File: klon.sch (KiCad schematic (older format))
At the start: 71 parts, among them SW1 SW_DPDT_x2, U1 TL072, U2 LTC1044, U3 TL072

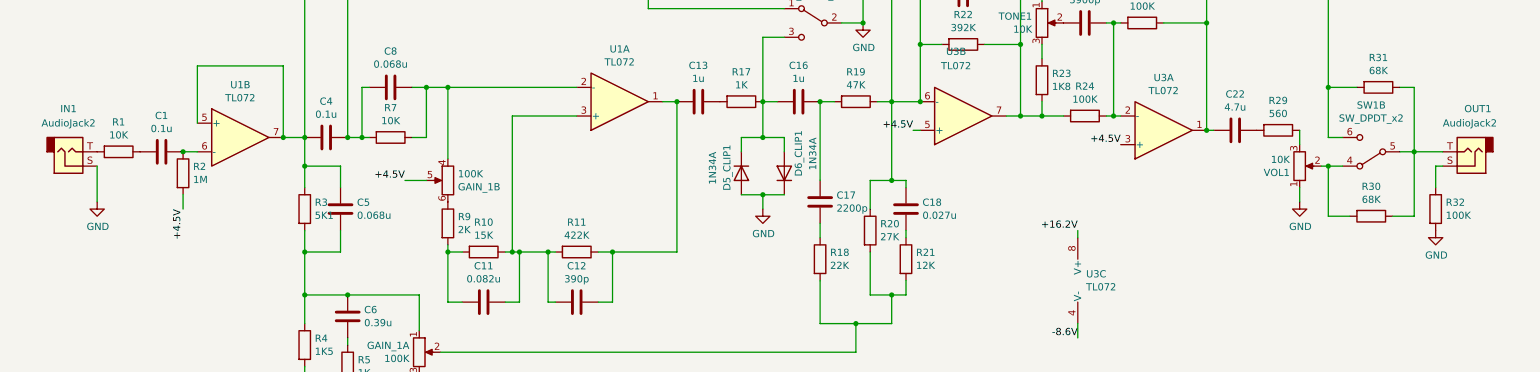
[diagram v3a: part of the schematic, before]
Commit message: add custom models, change pcb board layout
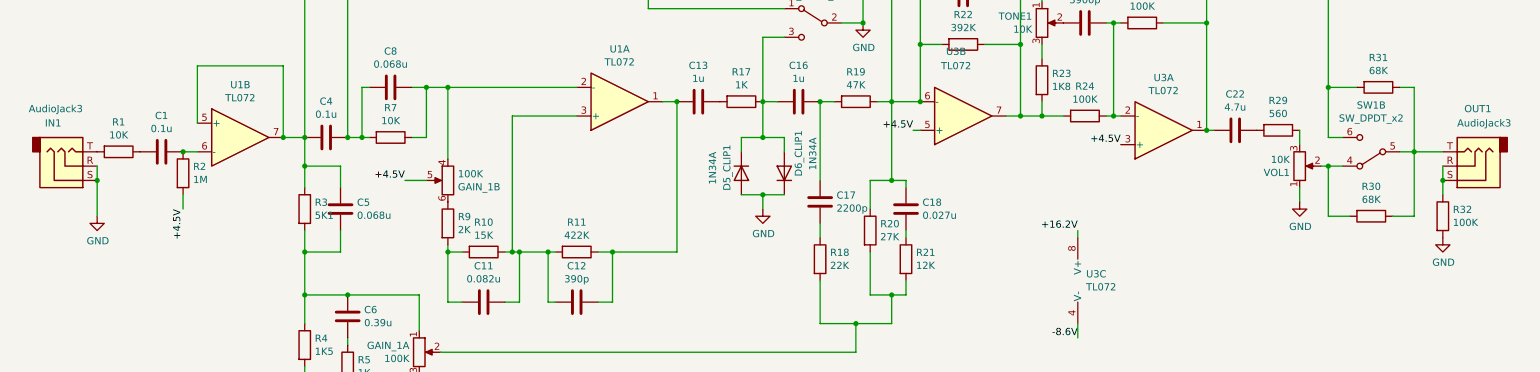
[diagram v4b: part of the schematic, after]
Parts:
- removed IN1, OUT1: AudioJack2, Connector_Audio:Jack_6.35mm_Neutrik_NMJ4HFD2_Horizontal, symbol Connector:AudioJack2
- added IN1, OUT1: AudioJack3, Connector_Audio:Jack_6.35mm_Neutrik_NMJ6HFD2_Horizontal, symbol Connector:AudioJack3
- GAIN_1: footprint Connector_PinHeader_1.27mm:PinHeader_2x03_P1.27mm_Vertical -> Potentiometer_THT:Potentiometer_Alpha_RD902F-40-00D_Dual_Vertical_CircularHoles
- TONE1, VOL1: footprint Connector_PinHeader_1.27mm:PinHeader_1x03_P1.27mm_Vertical -> Potentiometer_THT:Potentiometer_Alpha_RD901F-40-00D_Single_Vertical_CircularHoles
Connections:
- net GND: now also IN1.R, IN1.S
- net at R1.2: now also IN1.T
- net at R30.1, R31.1, SW1.5 (B): now also OUT1.T
- net at R32.1: now also OUT1.R, OUT1.S
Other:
- moved on the sheet: R32
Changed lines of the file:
@@
 F 0 "GAIN_1" H 3281 4846 50  0000 R CNN
 F 1 "100K" H 3281 4755 50  0000 R CNN
-F 2 "Connector_PinHeader_1.27mm:PinHeader_2x03_P1.27mm_Vertical" H 3350 4800 50  0001 C CNN
+F 2 "Potentiometer_THT:Potentiometer_Alpha_RD902F-40-00D_Dual_Vertical_CircularHoles" H 3350 4800 50  0001 C CNN
 F 3 "~" H 3350 4800 50  0001 C CNN
 	1    3350 4800
@@
 F 0 "TONE1" H 7631 2546 50  0000 R CNN
 F 1 "10K" H 7631 2455 50  0000 R CNN
-F 2 "Connector_PinHeader_1.27mm:PinHeader_1x03_P1.27mm_Vertical" H 7700 2500 50  0001 C CNN
+F 2 "Potentiometer_THT:Potentiometer_Alpha_RD901F-40-00D_Single_Vertical_CircularHoles" H 7700 2500 50  0001 C CNN
 F 3 "~" H 7700 2500 50  0001 C CNN
 	1    7700 2500
@@
 F 0 "VOL1" H 9431 3546 50  0000 R CNN
 F 1 "10K" H 9431 3455 50  0000 R CNN
-F 2 "Connector_PinHeader_1.27mm:PinHeader_1x03_P1.27mm_Vertical" H 9500 3500 50  0001 C CNN
+F 2 "Potentiometer_THT:Potentiometer_Alpha_RD901F-40-00D_Single_Vertical_CircularHoles" H 9500 3500 50  0001 C CNN
 F 3 "~" H 9500 3500 50  0001 C CNN
 	1    9500 3500
@@
 L Device:R R32
 U 1 1 60E3FE02
-P 10450 3800
-F 0 "R32" H 10520 3846 50  0000 L CNN
-F 1 "100K" H 10520 3755 50  0000 L CNN
-F 2 "Resistor_THT:R_Axial_DIN0207_L6.3mm_D2.5mm_P10.16mm_Horizontal" V 10380 3800 50  0001 C CNN
-F 3 "~" H 10450 3800 50  0001 C CNN
-	1    10450 3800
+P 10500 3850
+F 0 "R32" H 10570 3896 50  0000 L CNN
+F 1 "100K" H 10570 3805 50  0000 L CNN
+F 2 "Resistor_THT:R_Axial_DIN0207_L6.3mm_D2.5mm_P10.16mm_Horizontal" V 10430 3850 50  0001 C CNN
+F 3 "~" H 10500 3850 50  0001 C CNN
+	1    10500 3850
 	1    0    0    -1
 $EndComp
@@
 L power:GND #PWR017
 U 1 1 60E40ABE
-P 10450 3950
-F 0 "#PWR017" H 10450 3700 50  0001 C CNN
-F 1 "GND" H 10455 3777 50  0000 C CNN
-F 2 "" H 10450 3950 50  0001 C CNN
-F 3 "" H 10450 3950 50  0001 C CNN
-	1    10450 3950
+P 10500 4000
+F 0 "#PWR017" H 10500 3750 50  0001 C CNN
+F 1 "GND" H 10505 3827 50  0000 C CNN
+F 2 "" H 10500 4000 50  0001 C CNN
+F 3 "" H 10500 4000 50  0001 C CNN
+	1    10500 4000
 	1    0    0    -1
 $EndComp
@@
 Wire Wire Line
 	10150 3850 10300 3850
-$Comp
-L Connector:AudioJack2 OUT1
-U 1 1 60F6182B
-P 10700 3400
-F 0 "OUT1" H 10750 3100 50  0000 R CNN
-F 1 "AudioJack2" H 10900 3200 50  0000 R CNN
-F 2 "Connector_Audio:Jack_6.35mm_Neutrik_NMJ4HFD2_Horizontal" H 10700 3400 50  0001 C CNN
-F 3 "~" H 10700 3400 50  0001 C CNN
-	1    10700 3400
-	-1   0    0    1
-$EndComp
-$Comp
-L Connector:AudioJack2 IN1
-U 1 1 60F62CED
-P 900 3400
-F 0 "IN1" H 900 3100 50  0000 C CNN
-F 1 "AudioJack2" H 900 3200 50  0000 C CNN
-F 2 "Connector_Audio:Jack_6.35mm_Neutrik_NMJ4HFD2_Horizontal" H 900 3400 50  0001 C CNN
-F 3 "~" H 900 3400 50  0001 C CNN
-	1    900  3400
-	1    0    0    1
-$EndComp
 Wire Wire Line
 	7550 3150 7700 3150
@@
 L power:GND #PWR01
 U 1 1 610974EE
-P 1100 3750
-F 0 "#PWR01" H 1100 3500 50  0001 C CNN
-F 1 "GND" H 1105 3577 50  0000 C CNN
-F 2 "" H 1100 3750 50  0001 C CNN
-F 3 "" H 1100 3750 50  0001 C CNN
-	1    1100 3750
-	1    0    0    -1
-$EndComp
-Wire Wire Line
-	1100 3750 1100 3500
+P 1100 3850
+F 0 "#PWR01" H 1100 3600 50  0001 C CNN
+F 1 "GND" H 1105 3677 50  0000 C CNN
+F 2 "" H 1100 3850 50  0001 C CNN
+F 3 "" H 1100 3850 50  0001 C CNN
+	1    1100 3850
+	1    0    0    -1
+$EndComp
+Wire Wire Line
+	1100 3850 1100 3600
 Wire Wire Line
 	1700 3400 1800 3400
@@
 Connection ~ 6850 3050
 Connection ~ 9700 2950
-Wire Wire Line
-	10500 3500 10450 3500
-Wire Wire Line
-	10450 3500 10450 3650
 Wire Wire Line
 	10300 3400 10500 3400
@@
 F 0 "GAIN_1" H 3480 3554 50  0000 R CNN
 F 1 "100K" H 3480 3645 50  0000 R CNN
-F 2 "Connector_PinHeader_1.27mm:PinHeader_2x03_P1.27mm_Vertical" H 3550 3600 50  0001 C CNN
+F 2 "Potentiometer_THT:Potentiometer_Alpha_RD902F-40-00D_Dual_Vertical_CircularHoles" H 3550 3600 50  0001 C CNN
 F 3 "~" H 3550 3600 50  0001 C CNN
 	2    3550 3600
@@
 Wire Wire Line
 	3100 5800 3450 5800
+$Comp
+L Connector:AudioJack3 IN1
+U 1 1 60E29C1F
+P 900 3500
+F 0 "IN1" H 850 3200 50  0000 R CNN
+F 1 "AudioJack3" H 1000 3100 50  0000 R CNN
+F 2 "Connector_Audio:Jack_6.35mm_Neutrik_NMJ6HFD2_Horizontal" H 900 3500 50  0001 C CNN
+F 3 "~" H 900 3500 50  0001 C CNN
+	1    900  3500
+	1    0    0    1
+$EndComp
+Wire Wire Line
+	1100 3600 1100 3500
+Connection ~ 1100 3600
+$Comp
+L Connector:AudioJack3 OUT1
+U 1 1 60E7EA09
+P 10700 3500
+F 0 "OUT1" H 10750 3100 50  0000 R CNN
+F 1 "AudioJack3" H 10800 3200 50  0000 R CNN
+F 2 "Connector_Audio:Jack_6.35mm_Neutrik_NMJ6HFD2_Horizontal" H 10700 3500 50  0001 C CNN
+F 3 "~" H 10700 3500 50  0001 C CNN
+	1    10700 3500
+	-1   0    0    1
+$EndComp
+Wire Wire Line
+	10500 3500 10500 3600
+Wire Wire Line
+	10500 3600 10500 3700
+Connection ~ 10500 3600
 $EndSCHEMATC

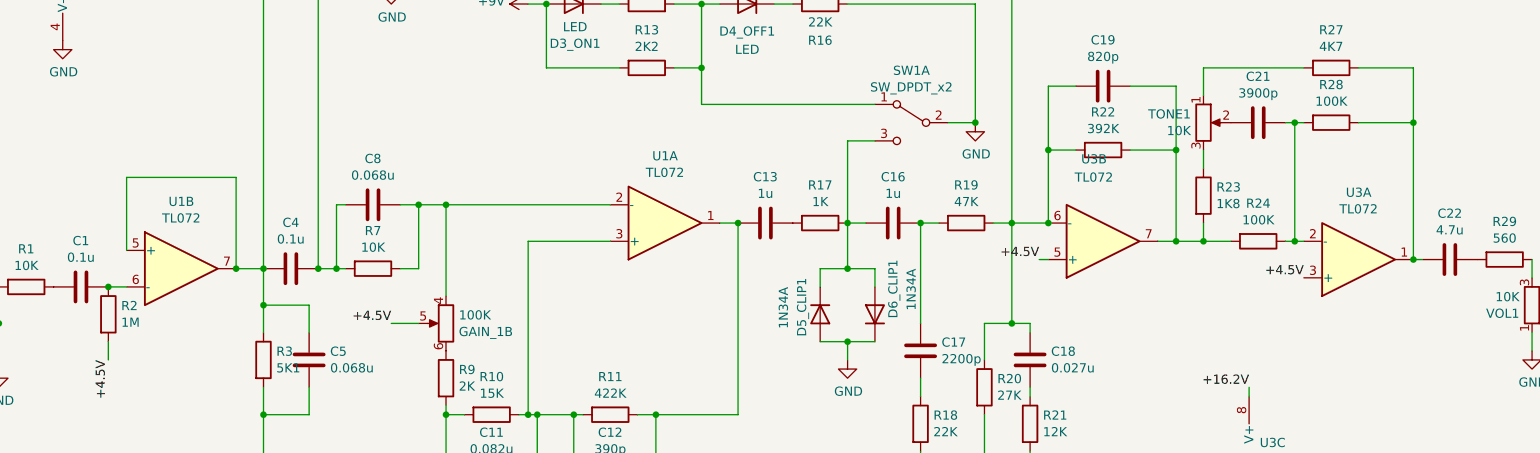
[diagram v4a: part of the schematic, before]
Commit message: optimize board to new dimensions
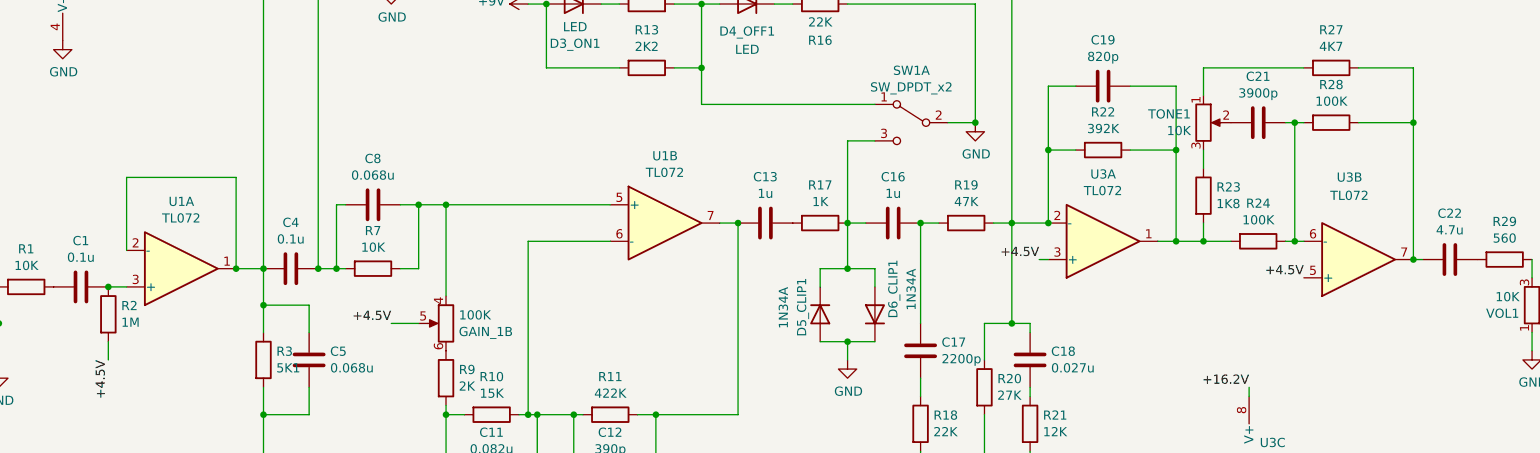
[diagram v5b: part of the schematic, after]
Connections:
- net at C1.1, R2.1: now also U1.3 (+); no longer U1.6 (-)
- net at C12.1, C13.2, R11.1: now also U1.7; no longer U1.1
- net at C8.1, GAIN_1.4, R7.1: now also U1.5 (+); no longer U1.2 (-)
- net at C11.1, C12.2, R10.1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: now also U1.6 (-); no longer U1.3 (+)
- net at C20.1, C4.2, C5.1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: now also U1.1, U1.2 (-); no longer U1.5 (+), U1.7
- net at C18.1, C19.2, R19.1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: now also U3.2 (-); no longer U3.6 (-)
- net at C22.2, R27.1, R28.1: now also U3.7; no longer U3.1
- net at C21.1, R24.1, R28.2: now also U3.6 (-); no longer U3.2 (-)
- net at C19.1, R22.1, R23.2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: now also U3.1; no longer U3.7
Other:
- moved on the sheet: U1A, U1B, U3A, U3B
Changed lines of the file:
@@
 L Amplifier_Operational:TL072 U1
 U 1 1 60C922E5
+P 2100 3300
+F 0 "U1" H 2100 2933 50  0000 C CNN
+F 1 "TL072" H 2100 3024 50  0000 C CNN
+F 2 "Package_DIP:DIP-8_W7.62mm" H 2100 3300 50  0001 C CNN
+F 3 "http://www.ti.com/lit/ds/symlink/tl071.pdf" H 2100 3300 50  0001 C CNN
+	1    2100 3300
+	1    0    0    1
+$EndComp
+$Comp
+L Amplifier_Operational:TL072 U1
+U 2 1 60C94D46
 P 4750 3050
-F 0 "U1" H 4750 2683 50  0000 C CNN
-F 1 "TL072" H 4750 2774 50  0000 C CNN
+F 0 "U1" H 4750 3417 50  0000 C CNN
+F 1 "TL072" H 4750 3326 50  0000 C CNN
 F 2 "Package_DIP:DIP-8_W7.62mm" H 4750 3050 50  0001 C CNN
 F 3 "http://www.ti.com/lit/ds/symlink/tl071.pdf" H 4750 3050 50  0001 C CNN
-	1    4750 3050
-	1    0    0    1
-$EndComp
-$Comp
-L Amplifier_Operational:TL072 U1
-U 2 1 60C94D46
-P 2100 3300
-F 0 "U1" H 2100 3667 50  0000 C CNN
-F 1 "TL072" H 2100 3576 50  0000 C CNN
-F 2 "Package_DIP:DIP-8_W7.62mm" H 2100 3300 50  0001 C CNN
-F 3 "http://www.ti.com/lit/ds/symlink/tl071.pdf" H 2100 3300 50  0001 C CNN
-	2    2100 3300
+	2    4750 3050
 	1    0    0    -1
 $EndComp
@@
 L Amplifier_Operational:TL072 U3
 U 1 1 60D072A8
-P 8550 3250
-F 0 "U3" H 8550 2883 50  0000 C CNN
-F 1 "TL072" H 8550 2974 50  0000 C CNN
-F 2 "Package_DIP:DIP-8_W7.62mm" H 8550 3250 50  0001 C CNN
-F 3 "http://www.ti.com/lit/ds/symlink/tl071.pdf" H 8550 3250 50  0001 C CNN
-	1    8550 3250
+P 7150 3150
+F 0 "U3" H 7150 2783 50  0000 C CNN
+F 1 "TL072" H 7150 2874 50  0000 C CNN
+F 2 "Package_DIP:DIP-8_W7.62mm" H 7150 3150 50  0001 C CNN
+F 3 "http://www.ti.com/lit/ds/symlink/tl071.pdf" H 7150 3150 50  0001 C CNN
+	1    7150 3150
 	1    0    0    1
 $EndComp
@@
 L Amplifier_Operational:TL072 U3
 U 2 1 60D097BC
-P 7150 3150
-F 0 "U3" H 7100 2700 50  0000 C CNN
-F 1 "TL072" H 7100 2800 50  0000 C CNN
-F 2 "Package_DIP:DIP-8_W7.62mm" H 7150 3150 50  0001 C CNN
-F 3 "http://www.ti.com/lit/ds/symlink/tl071.pdf" H 7150 3150 50  0001 C CNN
-	2    7150 3150
+P 8550 3250
+F 0 "U3" H 8500 2800 50  0000 C CNN
+F 1 "TL072" H 8500 2900 50  0000 C CNN
+F 2 "Package_DIP:DIP-8_W7.62mm" H 8550 3250 50  0001 C CNN
+F 3 "http://www.ti.com/lit/ds/symlink/tl071.pdf" H 8550 3250 50  0001 C CNN
+	2    8550 3250
 	1    0    0    1
 $EndComp
